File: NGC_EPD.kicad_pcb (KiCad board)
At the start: 2 copper layers, 10 parts, among them J1 Conn_ARM_JTAG_SWD_10, U1 NGC1081

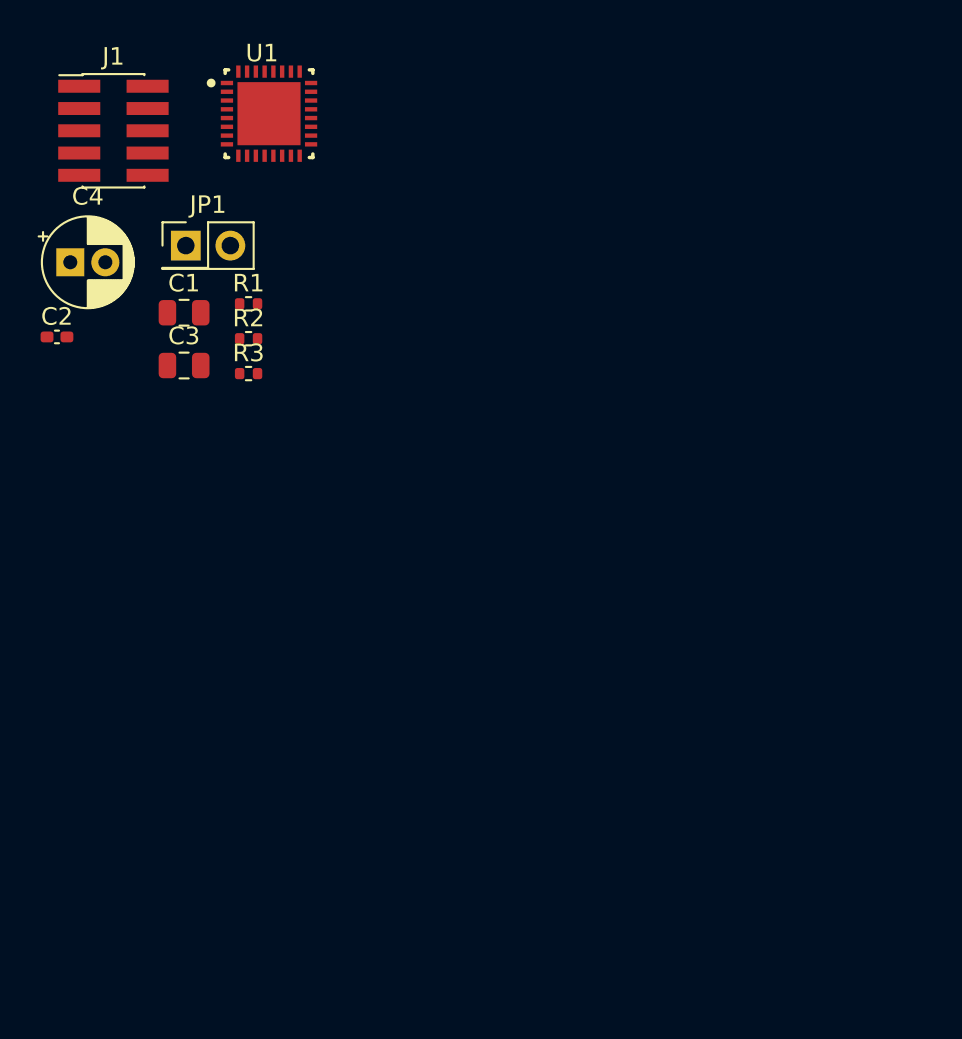
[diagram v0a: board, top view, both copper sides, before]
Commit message: Finished layout. Seperate antena board required.
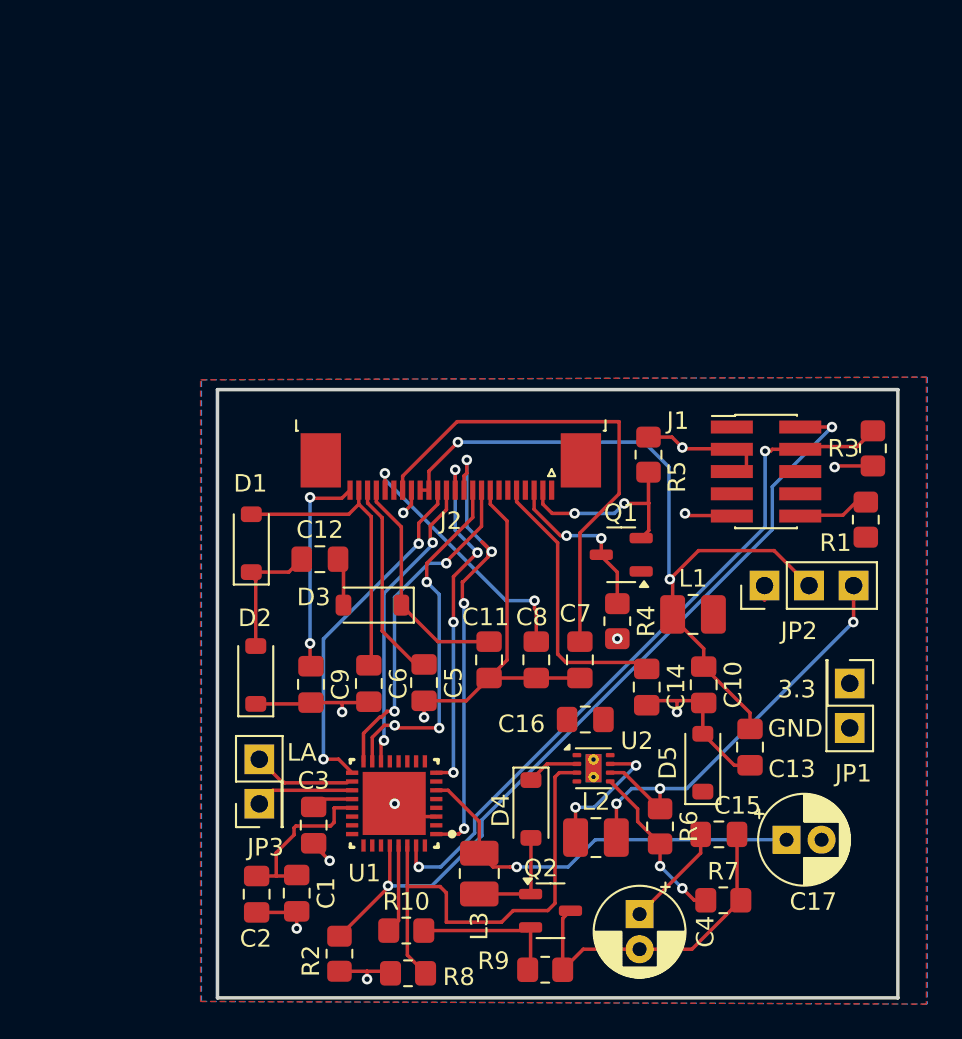
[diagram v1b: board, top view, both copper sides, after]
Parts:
- added C10: 1uF, Capacitor_SMD:C_0805_2012Metric_Pad1.18x1.45mm_HandSolder, F.Cu at (153.4, 100.9)
- added C11: 1uF, Capacitor_SMD:C_0805_2012Metric_Pad1.18x1.45mm_HandSolder, F.Cu at (141.2, 99.4)
- added C12: 4.7uF, Capacitor_SMD:C_0805_2012Metric_Pad1.18x1.45mm_HandSolder, F.Cu at (131.5, 93.7)
- added C13: 4.7uF, Capacitor_SMD:C_0805_2012Metric_Pad1.18x1.45mm_HandSolder, F.Cu at (156.1, 104.4)
- added C14: 1uF, Capacitor_SMD:C_0805_2012Metric_Pad1.18x1.45mm_HandSolder, F.Cu at (150.2, 101.0)
- added C15: 10uF, Capacitor_SMD:C_0805_2012Metric_Pad1.18x1.45mm_HandSolder, F.Cu at (154.3, 109.4)
- added C16: 10uF, Capacitor_SMD:C_0805_2012Metric_Pad1.18x1.45mm_HandSolder, F.Cu at (146.7, 102.8)
- added C17: 1mF, Capacitor_THT:CP_Radial_D5.0mm_P2.00mm, F.Cu at (158.1, 109.7)
- added C5: 1uF, Capacitor_SMD:C_0805_2012Metric_Pad1.18x1.45mm_HandSolder, F.Cu at (137.5, 100.7)
- added C6: 1uF, Capacitor_SMD:C_0805_2012Metric_Pad1.18x1.45mm_HandSolder, F.Cu at (134.3, 100.8)
- added C7: 1uF, Capacitor_SMD:C_0805_2012Metric_Pad1.18x1.45mm_HandSolder, F.Cu at (146.4, 99.4)
- added C8: 1uF, Capacitor_SMD:C_0805_2012Metric_Pad1.18x1.45mm_HandSolder, F.Cu at (143.9, 99.4)
- added C9: 1uF, Capacitor_SMD:C_0805_2012Metric_Pad1.18x1.45mm_HandSolder, F.Cu at (131.0, 100.8)
- added D1: D, Diode_SMD:D_SOD-123, F.Cu at (127.6, 92.8)
- added D2: D, Diode_SMD:D_SOD-123, F.Cu at (127.9, 100.3)
- added D3: D, Diode_SMD:D_SOD-123, F.Cu at (134.5, 96.3)
- added D4: D_Schottky_Small, Diode_SMD:D_SOD-123, F.Cu at (143.6, 107.9)
- added D5: D_Zener_Small, Diode_SMD:D_SOD-123, F.Cu at (153.4, 105.3)
- added J2: EPD_FCC, Connector_FFC-FPC:TE_2-1734839-4_1x24-1MP_P0.5mm_Horizontal, F.Cu at (139.0, 88.4)
- added JP2: Jumper_3_Open, Connector_PinHeader_2.54mm:PinHeader_1x03_P2.54mm_Vertical, F.Cu at (156.9, 95.2)
- added JP3: ANT, Connector_PinHeader_2.54mm:PinHeader_2x01_P2.54mm_Vertical, F.Cu at (128.1, 107.7)
- added L1: 10uH, Inductor_SMD:L_1008_2520Metric_Pad1.43x2.20mm_HandSolder, F.Cu at (152.8, 96.8)
- added L2: 10uH, Inductor_SMD:L_1008_2520Metric_Pad1.43x2.20mm_HandSolder, F.Cu at (147.3, 109.6)
- added L3: 100uH, Inductor_SMD:L_1008_2520Metric_Pad1.43x2.20mm_HandSolder, F.Cu at (140.6, 111.6)
- added Q1: NMOS, Package_TO_SOT_SMD:SOT-23-3, F.Cu at (148.7, 93.4)
- added Q2: NMOS, Package_TO_SOT_SMD:SOT-23-3, F.Cu at (144.7, 113.7)
- added R10: 10, Resistor_SMD:R_0805_2012Metric_Pad1.20x1.40mm_HandSolder, F.Cu at (136.4, 114.9)
- added R4: 3, Resistor_SMD:R_0805_2012Metric_Pad1.20x1.40mm_HandSolder, F.Cu at (148.5, 97.2)
- added R5: 10K, Resistor_SMD:R_0805_2012Metric_Pad1.20x1.40mm_HandSolder, F.Cu at (150.3, 87.7)
- added R6: 1.8M, Resistor_SMD:R_0805_2012Metric_Pad1.20x1.40mm_HandSolder, F.Cu at (150.9, 108.9)
- added R7: 576K, Resistor_SMD:R_0805_2012Metric_Pad1.20x1.40mm_HandSolder, F.Cu at (154.5, 113.2)
- added R8: 100K, Resistor_SMD:R_0805_2012Metric_Pad1.20x1.40mm_HandSolder, F.Cu at (136.6, 117.3)
- added R9: 100K, Resistor_SMD:R_0805_2012Metric_Pad1.20x1.40mm_HandSolder, F.Cu at (144.4, 117.1)
- added U2: TPS62125DSG, Package_SON:WSON-8-1EP_2x2mm_P0.5mm_EP0.9x1.6mm_ThermalVias, F.Cu at (147.1, 105.6)
- C1: footprint Capacitor_SMD:C_0805_2012Metric -> Capacitor_SMD:C_0805_2012Metric_Pad1.18x1.45mm_HandSolder
- C2: footprint Capacitor_SMD:C_0402_1005Metric_Pad0.74x0.62mm_HandSolder -> Capacitor_SMD:C_0805_2012Metric_Pad1.18x1.45mm_HandSolder
- C3: value 1uF -> 2uF; footprint Capacitor_SMD:C_0805_2012Metric -> Capacitor_SMD:C_0805_2012Metric_Pad1.18x1.45mm_HandSolder
- JP1: value Jumper_2_Open -> EXT_SUP
- R1, R2, R3: footprint Resistor_SMD:R_0402_1005Metric -> Resistor_SMD:R_0805_2012Metric_Pad1.20x1.40mm_HandSolder
- moved C4 49.4 mm to (149.8, 113.9), turned to -90 degrees
- moved JP1 45.4 mm to (161.7, 100.8), turned to -90 degrees
- moved J1 42.0 mm to (157.0, 88.7)
- moved U1 40.0 mm to (135.8, 107.6), turned to 180 degrees
- moved R1 37.3 mm to (162.7, 91.4), turned to 90 degrees
- moved R3 35.9 mm to (163.1, 87.4), turned to -90 degrees
- moved R2 35.5 mm to (132.6, 116.2), turned to -90 degrees
- moved C2 33.8 mm to (127.9, 112.8), turned to -90 degrees
- moved C1 33.7 mm to (130.2, 112.7), turned to -90 degrees
- moved C3 27.2 mm to (131.2, 108.9), turned to -90 degrees
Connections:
- net GND renamed BSI
- C4 pad 1: Net-(U1-VCC_HB) -> BOOST_OUT
- U1 pad 1: unconnected-(U1-GPIO4-Pad1) -> D/C#
- U1 pad 13: unconnected-(U1-GPIO9-Pad13) -> EPD_ENABLE
- U1 pad 14: unconnected-(U1-GPIO1-Pad14) -> SCL
- U1 pad 15: unconnected-(U1-GPIO8-Pad15) -> RES#
- U1 pad 16: unconnected-(U1-GPIO7-Pad16) -> BUSY
- U1 pad 17: unconnected-(U1-GPIO0-Pad17) -> SDA
- U1 pad 18: unconnected-(U1-LA-Pad18) -> Net-(JP3-B)
- U1 pad 19: unconnected-(U1-LB-Pad19) -> Net-(JP3-A)
- U1 pad 29: unconnected-(U1-GPIO15-Pad29) -> BOOST_PWM
- U1 pad 30: unconnected-(U1-GPIO14-Pad30) -> BUCK_EN
- U1 pad 6: Net-(U1-VCC_HB) -> VCC_HB
- U1 pad 8: unconnected-(U1-GPIO3-Pad8) -> CS#
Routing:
- net BSI: track 0.00 -> 83.3 mm, vias 0 -> 12
- net SWDIO: track 0.00 -> 46.3 mm, vias 0 -> 2
- net EPD3p3: track 0.00 -> 42.8 mm, vias 0 -> 2
- net SWDCLK: track 0.00 -> 39.8 mm, vias 0 -> 2
- net VDD: track 0.00 -> 27.9 mm
- net D/C#: track 0.00 -> 27.3 mm, vias 0 -> 4
- net BUCK_OUT: track 0.00 -> 27.0 mm, vias 0 -> 3
- net BUCK_EN: track 0.00 -> 27.0 mm
- net VCC_HB: track 0.00 -> 23.5 mm, vias 0 -> 1
- net CS#: track 0.00 -> 20.5 mm, vias 0 -> 4
- net RES#: track 0.00 -> 20.5 mm, vias 0 -> 3
- net SDA: track 0.00 -> 20.0 mm, vias 0 -> 2
- net BUSY: track 0.00 -> 19.2 mm, vias 0 -> 2
- net SCL: track 0.00 -> 17.1 mm, vias 0 -> 2
- net PREVGL: track 0.00 -> 16.7 mm
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- added copper zone on F.Cu, net +3.3V
- added copper zone on B.Cu, net BSI
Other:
- board outline added: 38.8 x 34.7 mm
- board text added: "3.3"
- board text added: "GND"
- board text added: "LA"

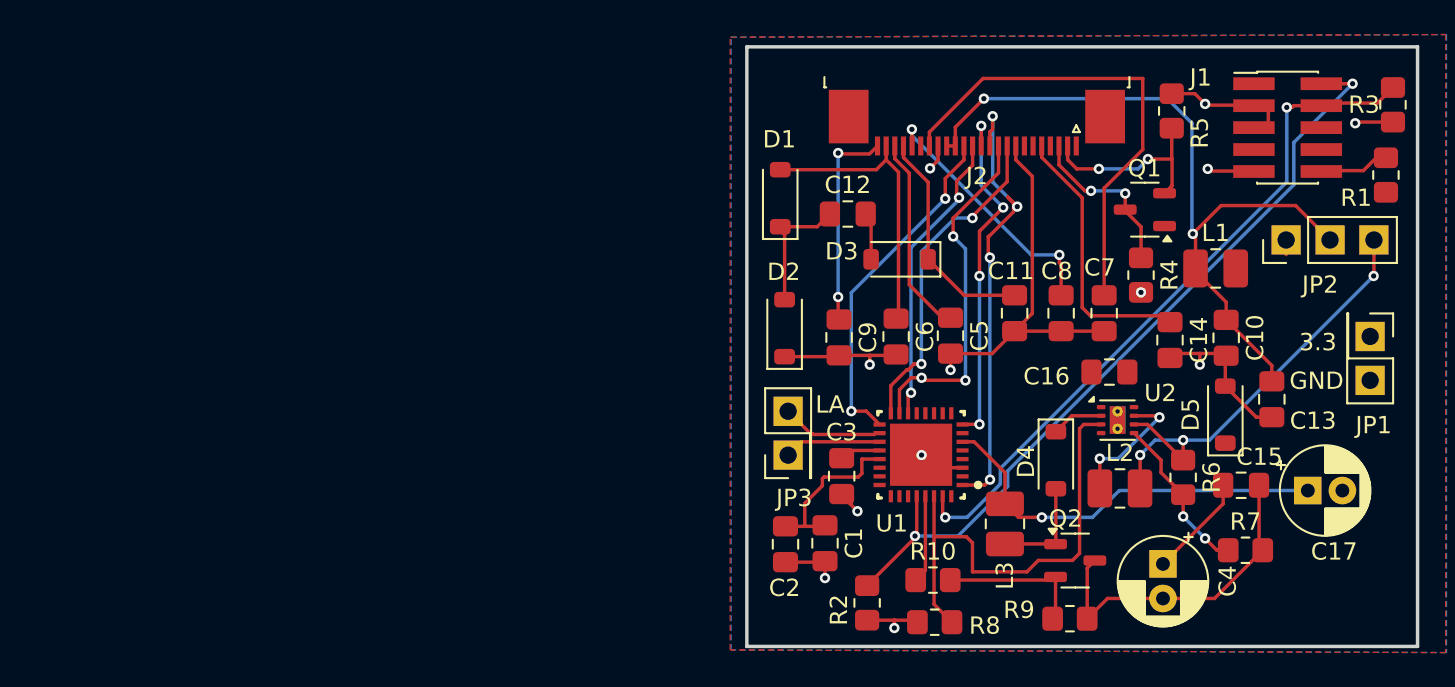
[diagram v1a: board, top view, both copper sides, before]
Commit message: Resolved PCD DRC errors. Added custom antenna. Need tuning of antenna.
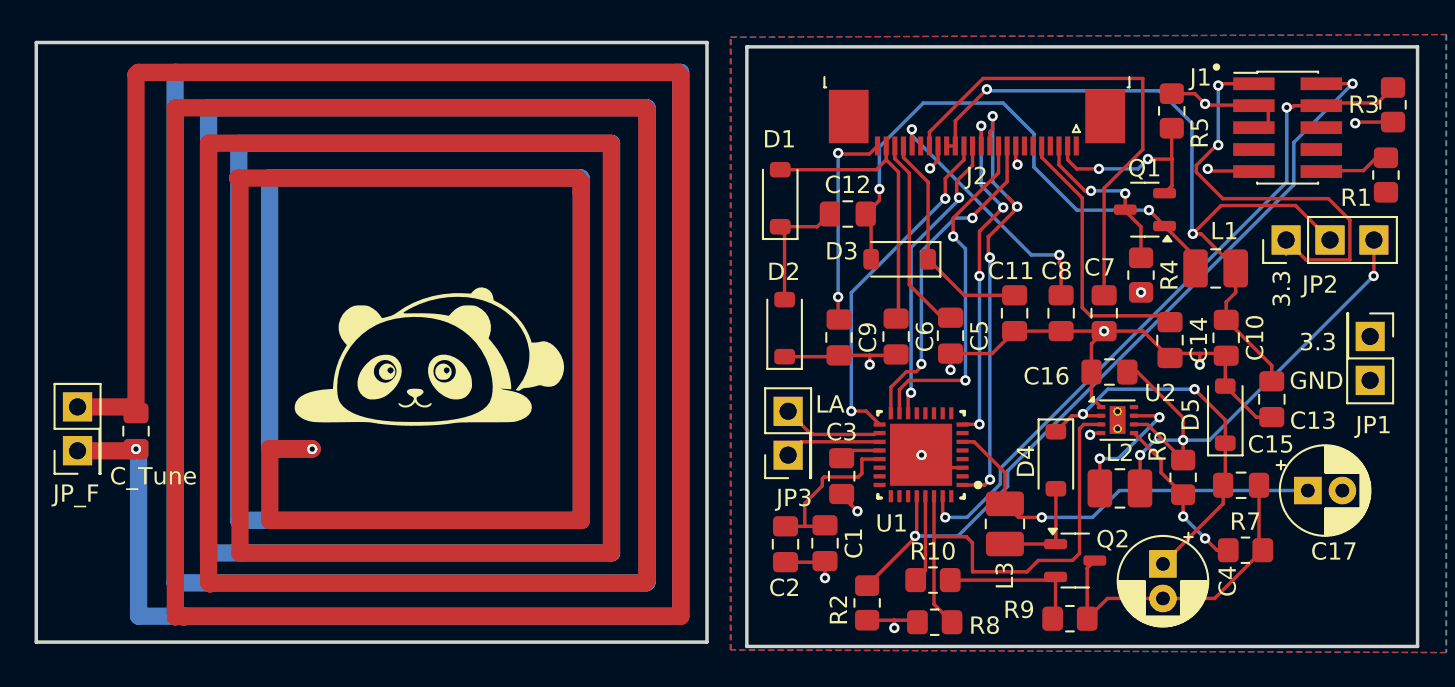
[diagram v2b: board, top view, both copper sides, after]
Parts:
- added C_Tune: 4.7uF, Capacitor_SMD:C_0805_2012Metric_Pad1.18x1.45mm_HandSolder, F.Cu at (90.3, 106.3)
- added G***: LOGO, LOGO, F.Cu at (107.3, 101.9)
- added JP_F: ANT, Connector_PinHeader_2.54mm:PinHeader_2x01_P2.54mm_Vertical, F.Cu at (86.9, 107.4)
- turned L1 to 180 degrees
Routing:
- net (no net): track 0.00 -> 811.7 mm, vias 0 -> 2
- net Net-(D3-A): track 2.75 -> 32.0 mm, vias 0 -> 2
- net +3.3V: track 10.6 -> 34.8 mm, vias 0 -> 2
- net BOOST_OUT: track 9.00 -> 22.4 mm, vias 0 -> 2
- net BUCK_OUT: track 27.0 -> 32.6 mm
- net EPD3p3: track 42.8 -> 44.5 mm
- net BSI: track 83.3 -> 83.0 mm, vias 12 -> 15
- net RES#: track 20.5 -> 20.4 mm, vias 3 -> 2
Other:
- board size 38.8 x 34.7 mm -> 79.9 x 34.9 mm

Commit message: Changed EPD FCC to backside. Added Testpoints and Infineon logo.
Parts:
- removed the G*** at (107.3, 101.9)
- added G***: LOGO, LOGO, F.Cu at (107.5, 100.8)
- added G***: LOGO, LOGO, B.Cu at (141.4, 114.9)
- added TP1: TestPoint, TestPoint:TestPoint_Pad_1.0x1.0mm, B.Cu at (130.4, 103.3)
- added TP2: TestPoint, TestPoint:TestPoint_Pad_1.0x1.0mm, B.Cu at (134.3, 100.8)
- added TP3: TestPoint, TestPoint:TestPoint_Pad_1.0x1.0mm, B.Cu at (137.4, 106.0)
- added TP4: TestPoint, TestPoint:TestPoint_Pad_1.0x1.0mm, B.Cu at (141.3, 104.3)
- added TP5: TestPoint, TestPoint:TestPoint_Pad_1.0x1.0mm, B.Cu at (137.5, 100.7)
- added TP6: TestPoint, TestPoint:TestPoint_Pad_1.0x1.0mm, F.Cu at (139.6, 115.8)
- J2: moved to B.Cu
- moved C5 4.33 mm to (141.6, 99.6)
- moved C11 2.58 mm to (138.6, 99.3)
- turned J2 to 0 degrees
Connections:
- net BSI renamed GND
- U1 pad 13: EPD_ENABLE -> unconnected-(U1-GPIO9-Pad13)
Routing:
- net +3.3V: track 34.8 -> 70.2 mm, vias 2 -> 3
- net PREVGL: track 16.7 -> 39.8 mm, vias 0 -> 1
- net SDA: track 20.0 -> 42.3 mm, vias 2 -> 1
- net SCL: track 17.1 -> 39.2 mm, vias 2 -> 1
- net GND: track 83.0 -> 101.9 mm, vias 15 -> 16
- net VDD: track 27.9 -> 10.7 mm, vias 0 -> 1
- net RESE: track 9.71 -> 23.3 mm, vias 2 -> 3
- net VCOM: track 12.1 -> 24.7 mm, vias 2 -> 1
- net GDR: track 11.3 -> 22.7 mm, vias 2 -> 1
- net VSH1: track 15.1 -> 9.54 mm, vias 2 -> 1
- net Net-(D3-A): track 32.0 -> 36.8 mm, vias 2 -> 0
- net VSH2: track 15.9 -> 20.5 mm, vias 0 -> 3
- net EPD3p3: track 44.5 -> 48.2 mm, vias 2 -> 0
- net D/C#: track 27.3 -> 24.1 mm, vias 4 -> 3
- net BUCK_EN: track 27.0 -> 29.6 mm
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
